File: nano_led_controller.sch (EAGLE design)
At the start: 9 parts, among them X1 JST-XH-03-PIN-LONG-PAD, X2 JST-XH-04-PIN-LONG-PAD

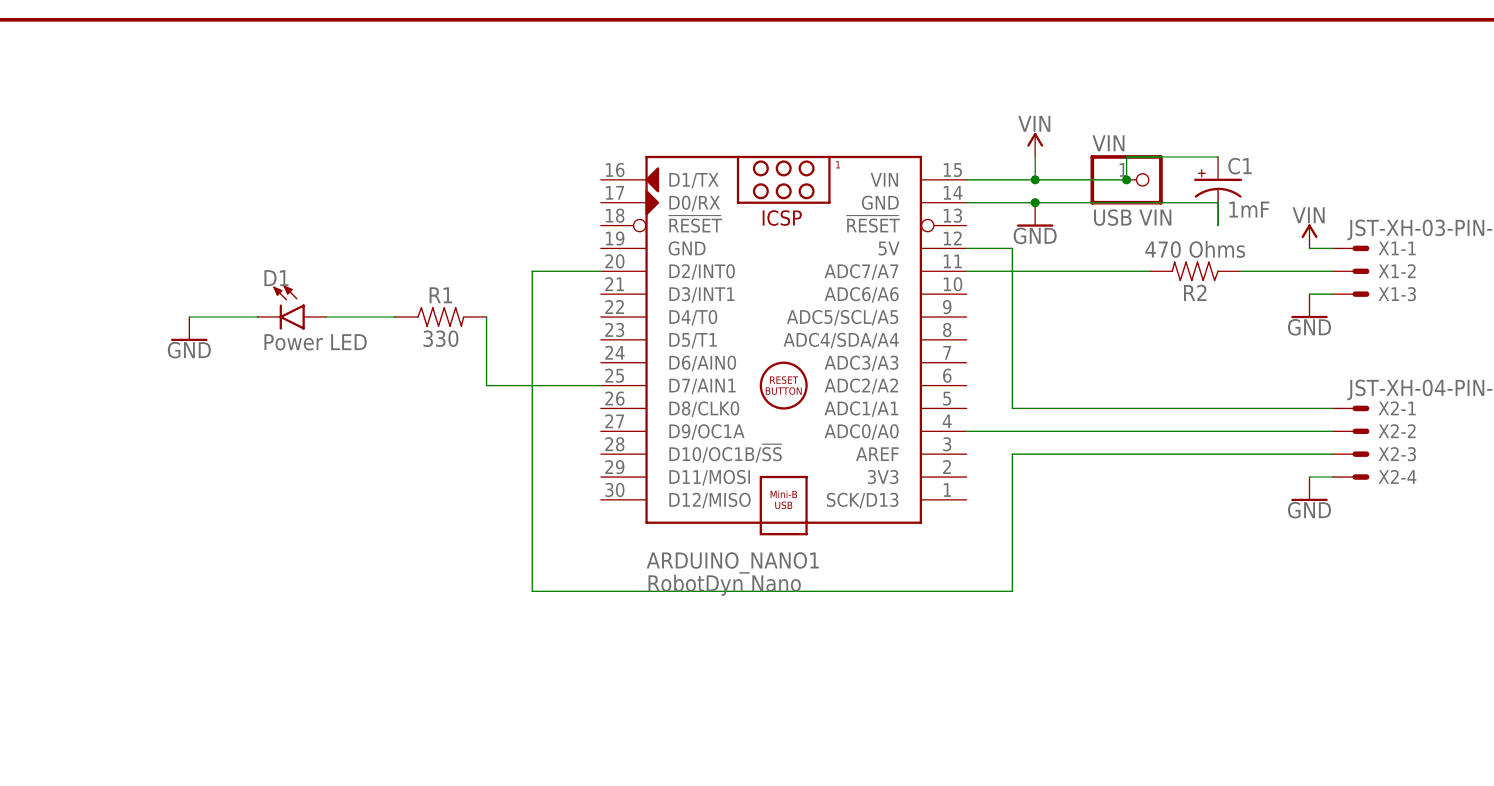
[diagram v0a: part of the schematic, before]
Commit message: Rearranged board to work with right angle USB cable
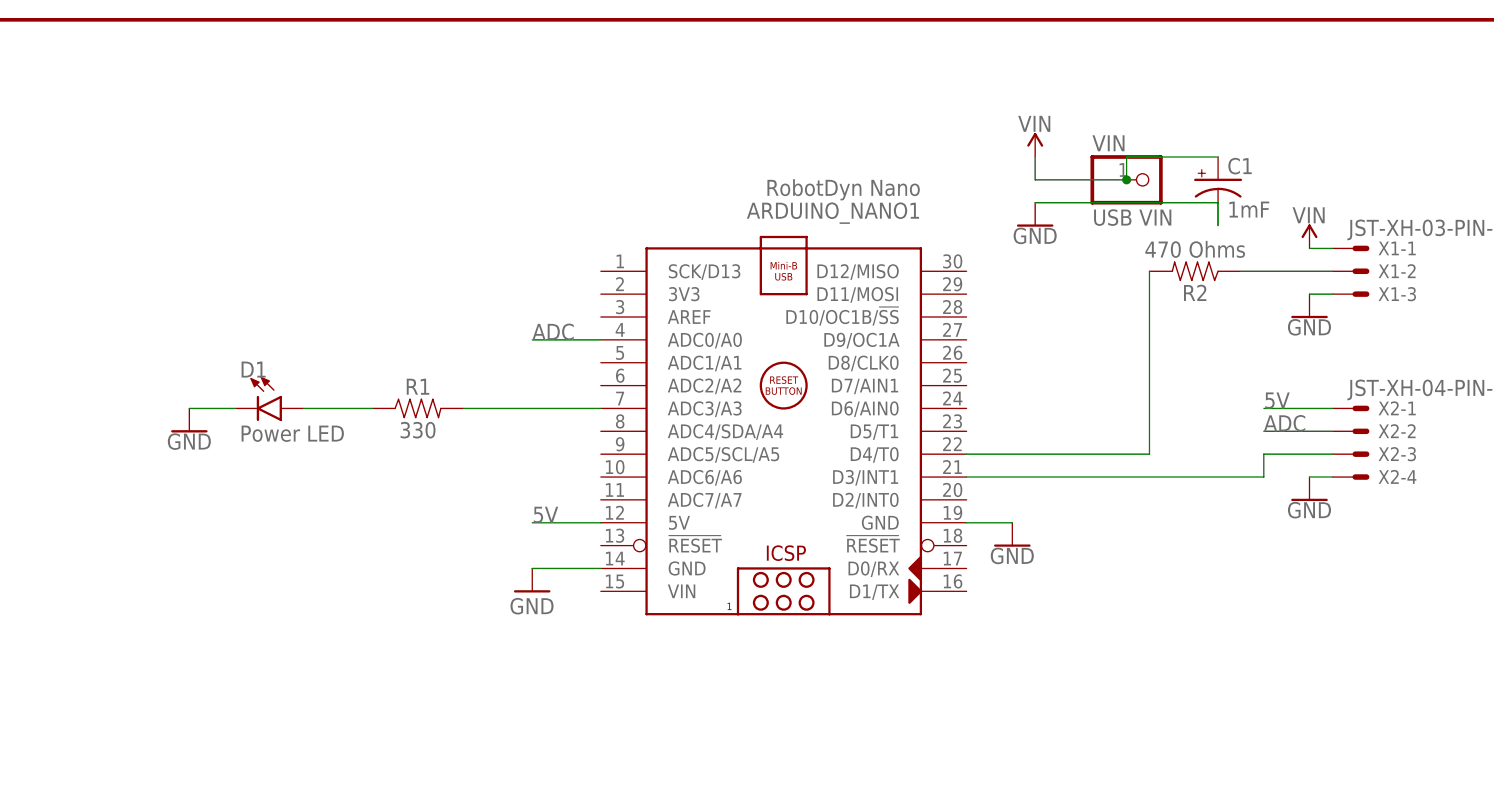
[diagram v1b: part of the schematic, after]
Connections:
- net N$3 renamed ADC
- removed net N$7: ARDUINO_NANO1.D7/AIN1, R1.2
- new net N$3: ARDUINO_NANO1.D4/T0, R2.2
- net GND: now also ARDUINO_NANO1.GND@1
- net N$1: now also ARDUINO_NANO1.ADC3/A3, R1.2; no longer ARDUINO_NANO1.ADC7/A7, R2.2
- net N$6: now also ARDUINO_NANO1.D3/INT1; no longer ARDUINO_NANO1.D2/INT0
- net VIN: no longer ARDUINO_NANO1.VIN
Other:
- moved on the sheet: ARDUINO_NANO1, D1, R1
